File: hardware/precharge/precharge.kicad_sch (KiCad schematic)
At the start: 39 parts, among them J1 Conn_01x02, J2 Conn_01x02, J3 Conn_01x02, J4 Conn_01x04, J5 Conn_01x03, J6 Conn_01x05, J7 Conn_01x02, U1 140817141410, U2 140817141410, U3 140817141410

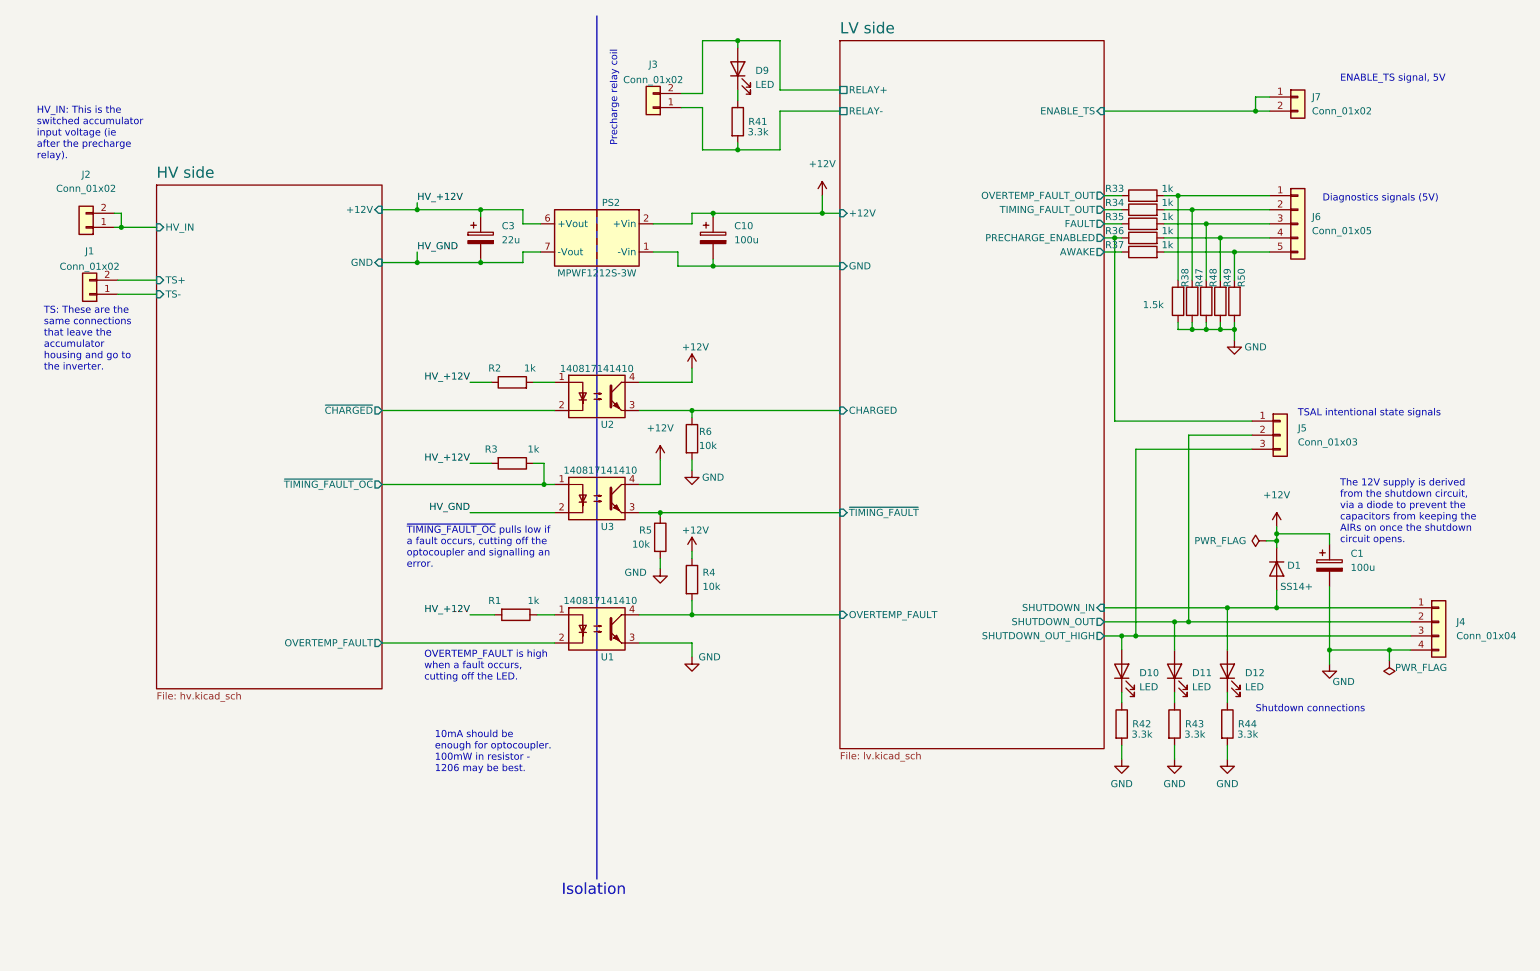
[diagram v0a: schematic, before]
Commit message: Added precharge layout
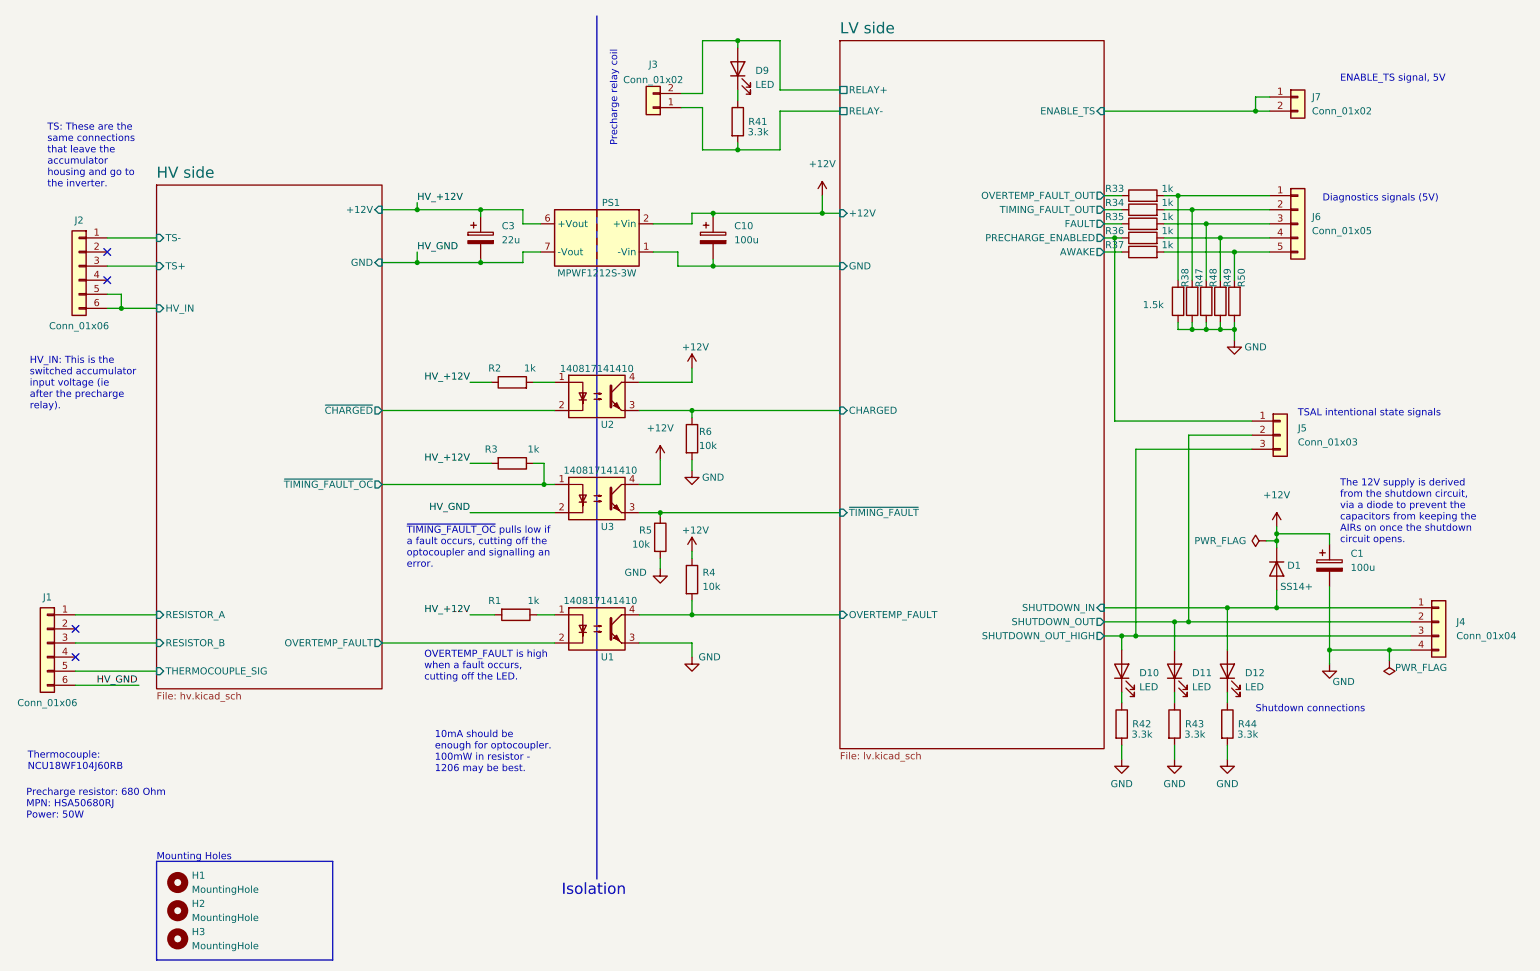
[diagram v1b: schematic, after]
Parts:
- removed J1, J2: Conn_01x02, Connector_Molex:Molex_Micro-Fit_3.0_43650-0200_1x02_P3.00mm_Horizontal, symbol Connector_Generic:Conn_01x02
- added H1, H2, H3: MountingHole, MountingHole:MountingHole_3.2mm_M3, symbol Mechanical:MountingHole
- added J1, J2: Conn_01x06, footprints:Molex_Micro-Fit_3.0_43650-0600_1x06_P3.00mm_Horizontal, symbol Connector_Generic:Conn_01x06
- J3, J7: footprint Connector_Molex:Molex_Micro-Fit_3.0_43650-0200_1x02_P3.00mm_Horizontal -> footprints:Molex_Micro-Fit_3.0_43650-0200_1x02_P3.00mm_Horizontal
- J4: footprint Connector_Molex:Molex_Micro-Fit_3.0_43650-0400_1x04_P3.00mm_Horizontal -> footprints:Molex_Micro-Fit_3.0_43650-0400_1x04_P3.00mm_Horizontal
- J5: footprint Connector_Molex:Molex_Micro-Fit_3.0_43650-0300_1x03_P3.00mm_Horizontal -> footprints:Molex_Micro-Fit_3.0_43650-0300_1x03_P3.00mm_Horizontal
- J6: footprint Connector_Molex:Molex_Micro-Fit_3.0_43650-0500_1x05_P3.00mm_Horizontal -> footprints:Molex_Micro-Fit_3.0_43650-0500_1x05_P3.00mm_Horizontal
- U1, U2, U3: footprint Package_DIP:DIP-4_W7.62mm -> footprints:DIP-4_W10.16mm
- renumbered PS2 to PS1
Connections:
- net HV side/HV_IN: now also J2.5 (Pin_5), J2.6 (Pin_6)
- net HV side/TS+: now also J2.3 (Pin_3)
- net HV side/TS-: now also J2.1 (Pin_1)
- net HV_GND: now also J1.6 (Pin_6)
- new net HV side/RESISTOR_A: J1.1 (Pin_1)
- new net HV side/RESISTOR_B: J1.3 (Pin_3)
- new net HV side/THERMOCOUPLE_SIG: J1.5 (Pin_5)
- no-connect marks 0 -> 4
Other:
- sheet HV side ports: added RESISTOR_A, RESISTOR_B, THERMOCOUPLE_SIG; removed none
- note added: "Mounting Holes"
- note added: "Precharge resistor: 680 Ohm MPN: HSA50680RJ Power: 50W"
- note added: "Thermocouple: NCU18WF104J60RB"
- title: (none) -> Precharge Top Level

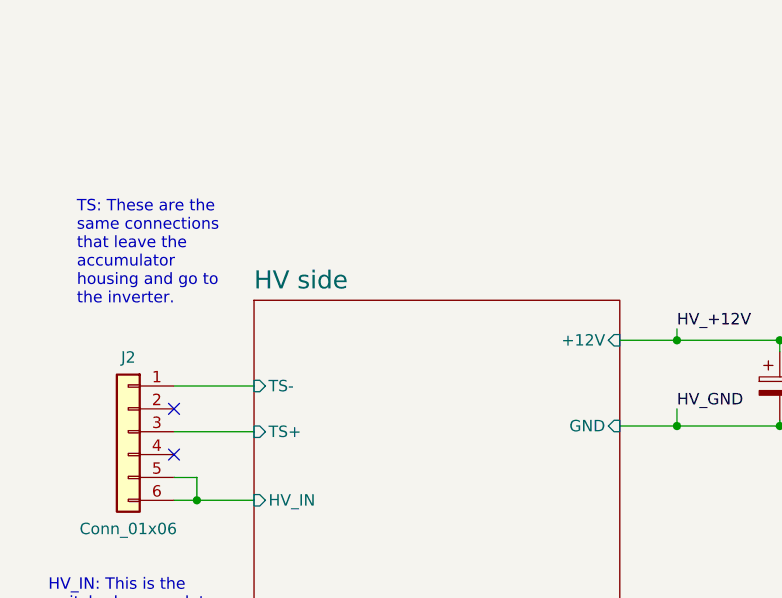
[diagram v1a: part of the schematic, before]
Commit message: Added initial indicator light
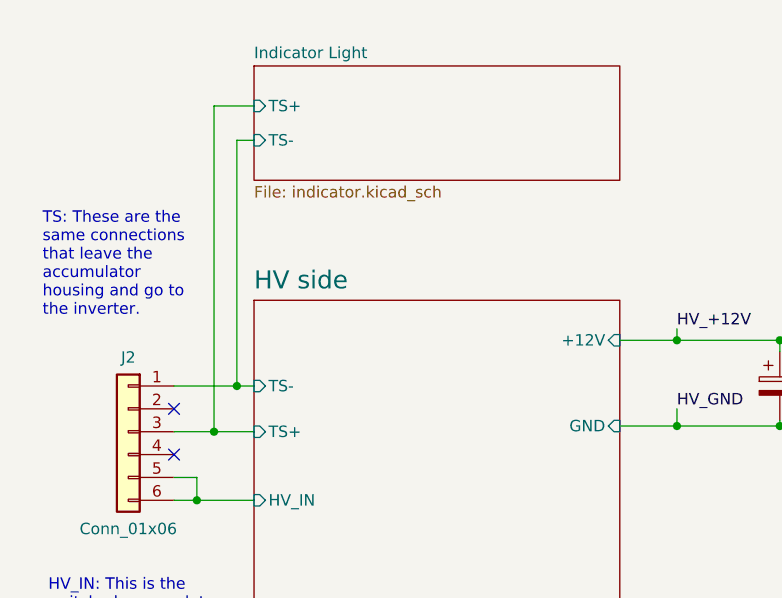
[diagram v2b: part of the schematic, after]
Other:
- added sheet Indicator Light (indicator.kicad_sch)
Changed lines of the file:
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@@
   (junction (at 229.87 79.375) (diameter 0) (color 0 0 0 0)
   )
+  (junction (at 33.655 67.945) (diameter 0) (color 0 0 0 0)
+  )
   (junction (at 212.09 134.62) (diameter 0) (color 0 0 0 0)
   )
@@
   )
   (junction (at 224.79 57.785) (diameter 0) (color 0 0 0 0)
+  )
+  (junction (at 36.195 62.865) (diameter 0) (color 0 0 0 0)
   )
   (junction (at 85.09 67.31) (diameter 0) (color 0 0 0 0)
@@
     (stroke (width 0) (type default) (color 0 0 0 0))
   )
+  (wire (pts (xy 36.195 35.56) (xy 38.1 35.56))
+    (stroke (width 0) (type default) (color 0 0 0 0))
+  )
   (wire (pts (xy 210.82 62.865) (xy 212.09 62.865))
     (stroke (width 0) (type default) (color 0 0 0 0))
@@
     (stroke (width 0) (type default) (color 0 0 0 0))
   )
+  (wire (pts (xy 36.195 62.865) (xy 38.1 62.865))
+    (stroke (width 0) (type default) (color 0 0 0 0))
+  )
   (wire (pts (xy 138.43 67.945) (xy 161.29 67.945))
     (stroke (width 0) (type default) (color 0 0 0 0))
@@
     (stroke (width 0) (type default) (color 0 0 0 0))
   )
-  (wire (pts (xy 29.21 62.865) (xy 38.1 62.865))
+  (wire (pts (xy 29.21 62.865) (xy 36.195 62.865))
     (stroke (width 0) (type default) (color 0 0 0 0))
   )
@@
     (stroke (width 0) (type default) (color 0 0 0 0))
   )
+  (wire (pts (xy 38.1 31.75) (xy 33.655 31.75))
+    (stroke (width 0) (type default) (color 0 0 0 0))
+  )
   (wire (pts (xy 208.915 55.245) (xy 212.09 55.245))
     (stroke (width 0) (type default) (color 0 0 0 0))
@@
     (stroke (width 0) (type default) (color 0 0 0 0))
   )
+  (wire (pts (xy 33.655 31.75) (xy 33.655 67.945))
+    (stroke (width 0) (type default) (color 0 0 0 0))
+  )
   (wire (pts (xy 23.495 140.97) (xy 38.1 140.97))
     (stroke (width 0) (type default) (color 0 0 0 0))
@@
     (stroke (width 0) (type default) (color 0 0 0 0))
   )
-  (wire (pts (xy 29.21 67.945) (xy 38.1 67.945))
+  (wire (pts (xy 29.21 67.945) (xy 33.655 67.945))
     (stroke (width 0) (type default) (color 0 0 0 0))
   )
@@
     (stroke (width 0) (type default) (color 0 0 0 0))
   )
+  (wire (pts (xy 33.655 67.945) (xy 38.1 67.945))
+    (stroke (width 0) (type default) (color 0 0 0 0))
+  )
   (wire (pts (xy 221.615 132.08) (xy 221.615 137.16))
     (stroke (width 0) (type default) (color 0 0 0 0))
@@
   )
   (wire (pts (xy 208.915 40.005) (xy 236.22 40.005))
+    (stroke (width 0) (type default) (color 0 0 0 0))
+  )
+  (wire (pts (xy 36.195 62.865) (xy 36.195 35.56))
     (stroke (width 0) (type default) (color 0 0 0 0))
   )
@@
   )
   (text "TS: These are the\nsame connections\nthat leave the\naccumulator\nhousing and go to\nthe inverter."
-    (at 18.415 53.975 0)
+    (at 14.605 55.245 0)
     (effects (font (size 1.27 1.27)) (justify left bottom))
   )
@@
     )
   )
+  (sheet (at 38.1 27.305) (size 40.64 12.7) (fields_autoplaced)
+    (stroke (width 0.1524) (type solid) (color 0 0 0 0))
+    (fill (color 0 0 0 0.0000))
+    (property "Sheet name" "Indicator Light" (id 0) (at 38.1 26.5934 0)
+      (effects (font (size 1.27 1.27)) (justify left bottom))
+    )
+    (property "Sheet file" "indicator.kicad_sch" (id 1) (at 38.1 40.5896 0)
+      (effects (font (size 1.27 1.27)) (justify left top))
+    )
+    (pin "TS+" input (at 38.1 31.75 180)
+      (effects (font (size 1.27 1.27)) (justify left))
+    )
+    (pin "TS-" input (at 38.1 35.56 180)
+      (effects (font (size 1.27 1.27)) (justify left))
+    )
+  )
   (sheet (at 161.29 27.305) (size 47.625 127.635) (fields_autoplaced)
     (stroke (width 0.1524) (type solid) (color 0 0 0 0))
@@
     (path "/86ebb052-21e6-4e49-945d-049a70338ab6" (page "2"))
     (path "/a25b3faf-d95a-49ad-9b40-7c3f8d869233" (page "3"))
+    (path "/9efa549b-079b-4747-bbda-5d5b1defcab0" (page "4"))
   )
   (symbol_instances
@@
       (reference "D16") (unit 1) (value "BAT54W") (footprint "Package_TO_SOT_SMD:SOT-323_SC-70")
     )
+    (path "/9efa549b-079b-4747-bbda-5d5b1defcab0/08ae0cd5-029b-4100-9008-bcd27e2408da"
+      (reference "D17") (unit 1) (value "BZX84C12L") (footprint "Package_TO_SOT_SMD:SOT-23")
+    )
+    (path "/9efa549b-079b-4747-bbda-5d5b1defcab0/fe0740b6-00ad-452f-b30f-7cad340fca5a"
+      (reference "D18") (unit 1) (value "BZX84C6V2L") (footprint "Package_TO_SOT_SMD:SOT-23")
+    )
     (path "/86ebb052-21e6-4e49-945d-049a70338ab6/9701a355-0600-47c8-8807-3e75f65e00ef"
       (reference "F1") (unit 1) (value "Fuse") (footprint "footprints:fuseholder")
@@
       (reference "J7") (unit 1) (value "Conn_01x02") (footprint "footprints:Molex_Micro-Fit_3.0_43650-0200_1x02_P3.00mm_Horizontal")
     )
+    (path "/9efa549b-079b-4747-bbda-5d5b1defcab0/40eac133-934e-4165-99e3-56e97f5fdc65"
+      (reference "J8") (unit 1) (value "LED") (footprint "footprints:Molex_Micro-Fit_3.0_43650-0200_1x02_P3.00mm_Horizontal")
+    )
     (path "/a25b3faf-d95a-49ad-9b40-7c3f8d869233/0eaa663a-c98d-44db-8bf5-70ab2ac22caf"
       (reference "K2") (unit 1) (value "G5Q-1EU DC12") (footprint "footprints:PCH-112L2MH")
@@
       (reference "Q7") (unit 1) (value "XP262N7002TR-G") (footprint "Package_TO_SOT_SMD:SOT-23")
     )
+    (path "/9efa549b-079b-4747-bbda-5d5b1defcab0/c4a37a2c-b29e-48bf-bc6a-dfd932617beb"
+      (reference "Q8") (unit 1) (value "FQD1N80TM") (footprint "Package_TO_SOT_SMD:TO-252-2")
+    )
+    (path "/9efa549b-079b-4747-bbda-5d5b1defcab0/a9d1e454-4d06-4e45-9e9b-c94eddcaee2b"
+      (reference "Q9") (unit 1) (value "XP262N7002TR-G") (footprint "Package_TO_SOT_SMD:SOT-23")
+    )
     (path "/88cf5644-d7d9-4547-9f60-58e416dff500"
       (reference "R1") (unit 1) (value "1k") (footprint "Resistor_SMD:R_1206_3216Metric")
@@
       (reference "R24") (unit 1) (value "100k") (footprint "Resistor_SMD:R_0603_1608Metric")
     )
+    (path "/9efa549b-079b-4747-bbda-5d5b1defcab0/2ff3ab08-bb18-487c-826d-64131b0657b4"
+      (reference "R25") (unit 1) (value "200k") (footprint "Resistor_SMD:R_0805_2012Metric")
+    )
     (path "/86ebb052-21e6-4e49-945d-049a70338ab6/f99d9765-47b3-46d8-b421-2c5b27dab9dd"
       (reference "R26") (unit 1) (value "33k") (footprint "Resistor_SMD:R_0603_1608Metric")
@@
       (reference "R63") (unit 1) (value "453k") (footprint "Resistor_SMD:R_0805_2012Metric")
     )
+    (path "/9efa549b-079b-4747-bbda-5d5b1defcab0/885b7918-6fc0-4356-a9c4-4493dc8395b7"
+      (reference "R64") (unit 1) (value "200k") (footprint "Resistor_SMD:R_0805_2012Metric")
+    )
+    (path "/9efa549b-079b-4747-bbda-5d5b1defcab0/a548cdaf-2e20-448f-ac62-9bd51c1fb9da"
+      (reference "R65") (unit 1) (value "200k") (footprint "Resistor_SMD:R_0805_2012Metric")
+    )
+    (path "/9efa549b-079b-4747-bbda-5d5b1defcab0/120de6b3-27d9-4070-8bbf-0273c903ffdf"
+      (reference "R66") (unit 1) (value "200k") (footprint "Resistor_SMD:R_0805_2012Metric")
+    )
+    (path "/9efa549b-079b-4747-bbda-5d5b1defcab0/d09db827-9281-452a-9907-71875c86f5cc"
+      (reference "R67") (unit 1) (value "200k") (footprint "Resistor_SMD:R_0805_2012Metric")
+    )
+    (path "/9efa549b-079b-4747-bbda-5d5b1defcab0/3aefe631-96c3-43fc-a61b-602bc7690a05"
+      (reference "R68") (unit 1) (value "470") (footprint "Resistor_SMD:R_0603_1608Metric")
+    )
+    (path "/9efa549b-079b-4747-bbda-5d5b1defcab0/d1790e9d-31f9-4ab3-ab76-b2a5e66c9cc9"
+      (reference "R69") (unit 1) (value "900k") (footprint "Resistor_SMD:R_0603_1608Metric")
+    )
+    (path "/9efa549b-079b-4747-bbda-5d5b1defcab0/6c658352-1319-4039-bf9e-7f5bf0207e87"
+      (reference "R70") (unit 1) (value "110k") (footprint "Resistor_SMD:R_0603_1608Metric")
+    )
+    (path "/9efa549b-079b-4747-bbda-5d5b1defcab0/06a589fb-bd37-4d32-b272-b9347d11949b"
+      (reference "R71") (unit 1) (value "4.7k") (footprint "Resistor_SMD:R_0603_1608Metric")
+    )
     (path "/152e40f8-eb06-4e19-ae6e-863e39431dd4"
       (reference "U1") (unit 1) (value "140817141410") (footprint "footprints:DIP-4_W10.16mm")
@@
       (reference "U5") (unit 7) (value "40106") (footprint "Package_SO:SOIC-14_3.9x8.7mm_P1.27mm")
     )
+    (path "/9efa549b-079b-4747-bbda-5d5b1defcab0/16c25b22-5d69-4c97-859d-7c6dd3465461"
+      (reference "U6") (unit 1) (value "OP777") (footprint "Package_SO:SOIC-8_3.9x4.9mm_P1.27mm")
+    )
     (path "/a25b3faf-d95a-49ad-9b40-7c3f8d869233/926d1ce2-3102-41b2-b331-fc5e7992978c"

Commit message: Latest precharge updates
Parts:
- removed PS1: MPWF1212S-3W, footprints:MPWF1212S-3W, symbol Converter_DCDC:ITX1212SA
- added PS1: 0.5S7B_1212S3UP, footprints:0.5S7B_1212S3UP, symbol symbols:0.5S7B_1212S3UP
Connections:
- net +12V: now also PS1.1 (+Vin)
- net HV_+12V: now also PS1.7 (+Vout)
- net HV_GND: now also PS1.5 (-Vout)
- net LV side/GND: now also PS1.2 (-Vin)
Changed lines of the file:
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@@
     (pin "2")
-  )
-  (symbol (lib_id "Converter_DCDC:ITX1212SA") (at 117.475 62.865 0) (mirror y) (unit 1)
-    (in_bom yes) (on_board yes)
-    (property "Reference" "PS1" (id 0) (at 120.015 56.515 0))
-    (property "Value" "MPWF1212S-3W" (id 1) (at 117.475 69.215 0))
-    (property "Footprint" "footprints:MPWF1212S-3W" (id 2) (at 144.145 69.215 0)
-      (effects (font (size 1.27 1.27)) (justify left) hide)
-    )
-    (property "Datasheet" "https://www.xppower.com/pdfs/SF_ITX.pdf" (id 3) (at 90.805 70.485 0)
-      (effects (font (size 1.27 1.27)) (justify left) hide)
-    )
-    (pin "1")
-    (pin "2")
-    (pin "6")
-    (pin "7")
-    (pin "8")
   )
   (symbol (lib_id "power:PWR_FLAG") (at 260.35 139.065 180) (unit 1)
@@
     (pin "1")
     (pin "2")
+  )
+  (symbol (lib_id "symbols:0.5S7B_1212S3UP") (at 117.475 62.865 0) (mirror y) (unit 1)
+    (in_bom yes) (on_board yes)
+    (property "Reference" "PS1" (id 0) (at 117.475 56.515 0))
+    (property "Value" "0.5S7B_1212S3UP" (id 1) (at 117.475 69.215 0))
+    (property "Footprint" "footprints:0.5S7B_1212S3UP" (id 2) (at 90.805 69.215 0)
+      (effects (font (size 1.27 1.27)) (justify left) hide)
+    )
+    (property "Datasheet" "https://www.xppower.com/pdfs/SF_ITX.pdf" (id 3) (at 144.145 70.485 0)
+      (effects (font (size 1.27 1.27)) (justify left) hide)
+    )
+    (pin "1")
+    (pin "2")
+    (pin "5")
+    (pin "7")
   )
   (sheet (at 38.1 53.34) (size 40.64 90.805) (fields_autoplaced)
@@
       (reference "D16") (unit 1) (value "BAT54W") (footprint "Package_TO_SOT_SMD:SOT-323_SC-70")
     )
-    (path "/9efa549b-079b-4747-bbda-5d5b1defcab0/08ae0cd5-029b-4100-9008-bcd27e2408da"
-      (reference "D17") (unit 1) (value "BZX84C12L") (footprint "Package_TO_SOT_SMD:SOT-23")
-    )
-    (path "/9efa549b-079b-4747-bbda-5d5b1defcab0/fe0740b6-00ad-452f-b30f-7cad340fca5a"
-      (reference "D18") (unit 1) (value "BZX84C6V2L") (footprint "Package_TO_SOT_SMD:SOT-23")
+    (path "/9efa549b-079b-4747-bbda-5d5b1defcab0/00e10c1c-cd66-4219-b3ad-1a69d3d3ac3e"
+      (reference "D17") (unit 1) (value "MMSZ4699T1G") (footprint "Diode_SMD:D_SOD-123")
+    )
+    (path "/9efa549b-079b-4747-bbda-5d5b1defcab0/c41b1f48-fa64-414b-99ce-7b568b8d4292"
+      (reference "D18") (unit 1) (value "MMSZ4691T1G") (footprint "Diode_SMD:D_SOD-123")
     )
     (path "/86ebb052-21e6-4e49-945d-049a70338ab6/9701a355-0600-47c8-8807-3e75f65e00ef"
@@
       (reference "NT2") (unit 1) (value "NetTie_2") (footprint "NetTie:NetTie-2_SMD_Pad0.5mm")
     )
-    (path "/c5d806ca-0b35-4110-8c45-5e6f271988fa"
-      (reference "PS1") (unit 1) (value "MPWF1212S-3W") (footprint "footprints:MPWF1212S-3W")
+    (path "/ff5091cc-f853-4b3b-8065-0371a79b8b29"
+      (reference "PS1") (unit 1) (value "0.5S7B_1212S3UP") (footprint "footprints:0.5S7B_1212S3UP")
     )
     (path "/86ebb052-21e6-4e49-945d-049a70338ab6/6a8b34e3-ef32-40ec-ad4f-2e5285dd56ee"
